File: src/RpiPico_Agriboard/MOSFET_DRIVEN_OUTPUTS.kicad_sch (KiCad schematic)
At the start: 7 parts, among them J12 Conn_02x03_Odd_Even, J23 Screw_Terminal_01x02, Q5 AP3404

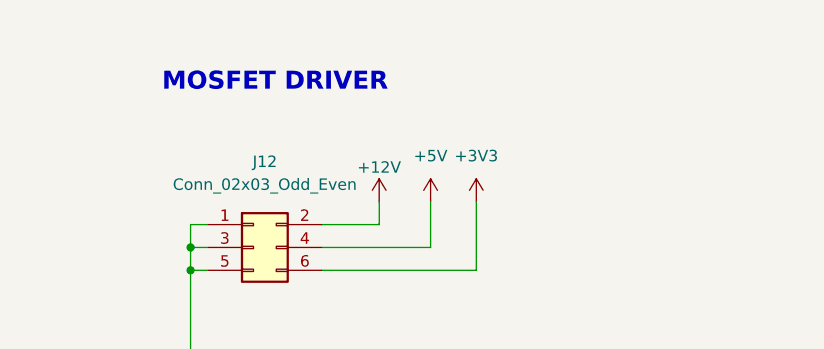
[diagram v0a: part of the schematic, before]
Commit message: complete board update and routing
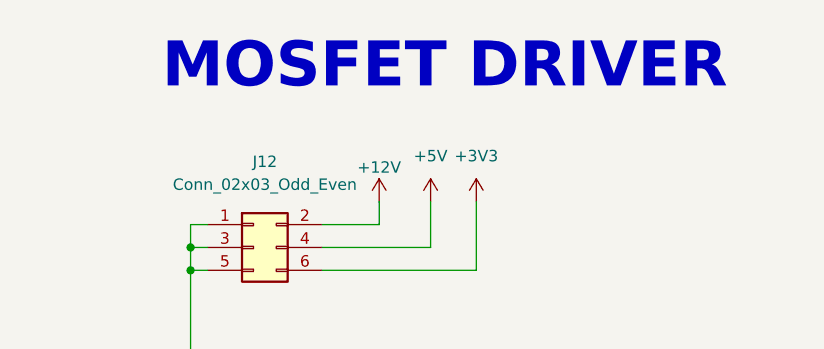
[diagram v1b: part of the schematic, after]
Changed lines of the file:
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@@
   )
   (text "MOSFET DRIVER" (at 126.365 27.94 0)
-    (effects (font (size 2 2) (thickness 0.4) bold) (justify left bottom))
+    (effects (font (face "Agency FB") (size 5 5) (thickness 0.4) bold) (justify left bottom))
   )
   (text "CURRENT LIMITING RESISTOR\n2A" (at 139.7 80.01 0)
